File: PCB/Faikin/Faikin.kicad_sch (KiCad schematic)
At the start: 26 parts, among them J1 1x5, J2 Shelly, J3 USB-PROG, Q1 BSS138PS, U2 ESP32-S3-MINI-1, U3 MD8942

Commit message: ERC check fixes
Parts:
- Q1: LCSC Part # C2912548 -> C193381
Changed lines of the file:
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@@
     (effects (font (size 1.27 1.27)) (justify left bottom))
   )
-  (global_label "DC" (shape input) (at 114.935 132.08 0) (fields_autoplaced)
+  (global_label "DC" (shape output) (at 114.935 132.08 0) (fields_autoplaced)
     (effects (font (size 1.27 1.27)) (justify left))
     (property "Intersheetrefs" "${INTERSHEET_REFS}" (at 119.806 132.08 0)
@@
     )
   )
-  (symbol (lib_name "GND_1") (lib_id "power:GND") (at 48.895 81.28 270) (unit 1)
+  (symbol (lib_id "power:GND") (at 48.895 81.28 270) (unit 1)
     (in_bom yes) (on_board yes) (dnp no) (fields_autoplaced)
     (property "Reference" "#PWR01" (at 42.545 81.28 0)
@@
     )
   )
-  (symbol (lib_name "GND_1") (lib_id "power:GND") (at 48.895 76.2 270) (unit 1)
+  (symbol (lib_id "power:GND") (at 48.895 76.2 270) (unit 1)
     (in_bom yes) (on_board yes) (dnp no) (fields_autoplaced)
     (property "Reference" "#PWR01" (at 42.545 76.2 0)
@@
     )
   )
-  (symbol (lib_name "BSS138PS_1") (lib_id "RevK:BSS138PS") (at 123.825 80.645 0) (unit 2)
+  (symbol (lib_id "RevK:BSS138PS") (at 123.825 80.645 0) (unit 2)
     (in_bom yes) (on_board yes) (dnp no)
     (property "Reference" "Q1" (at 122.555 75.565 0)
@@
       (effects (font (size 1.27 1.27)) hide)
     )
-    (property "LCSC Part #" "C2912548" (at 133.35 74.676 0)
+    (property "LCSC Part #" "C193381" (at 133.35 74.676 0)
       (effects (font (size 1.27 1.27)) hide)
     )
@@
     )
   )
-  (symbol (lib_name "GND_1") (lib_id "power:GND") (at 79.375 58.42 90) (unit 1)
+  (symbol (lib_id "power:GND") (at 79.375 58.42 90) (unit 1)
     (in_bom yes) (on_board yes) (dnp no) (fields_autoplaced)
     (property "Reference" "#PWR01" (at 85.725 58.42 0)
@@
     )
   )
-  (symbol (lib_name "GND_1") (lib_id "power:GND") (at 48.895 88.9 270) (unit 1)
+  (symbol (lib_id "power:GND") (at 48.895 88.9 270) (unit 1)
     (in_bom yes) (on_board yes) (dnp no) (fields_autoplaced)
     (property "Reference" "#PWR01" (at 42.545 88.9 0)
@@
     )
   )
-  (symbol (lib_name "GND_1") (lib_id "power:GND") (at 48.895 86.36 270) (unit 1)
+  (symbol (lib_id "power:GND") (at 48.895 86.36 270) (unit 1)
     (in_bom yes) (on_board yes) (dnp no) (fields_autoplaced)
     (property "Reference" "#PWR01" (at 42.545 86.36 0)
@@
       (effects (font (size 1.27 1.27)) hide)
     )
-    (property "LCSC Part #" "C2912548" (at 117.475 94.996 0)
+    (property "LCSC Part #" "C193381" (at 117.475 94.996 0)
       (effects (font (size 1.27 1.27)) hide)
     )
@@
     )
   )
-  (symbol (lib_name "GND_1") (lib_id "power:GND") (at 48.895 83.82 270) (unit 1)
+  (symbol (lib_id "power:GND") (at 48.895 83.82 270) (unit 1)
     (in_bom yes) (on_board yes) (dnp no) (fields_autoplaced)
     (property "Reference" "#PWR01" (at 42.545 83.82 0)
@@
     )
   )
-  (symbol (lib_name "GND_1") (lib_id "power:GND") (at 48.895 91.44 270) (unit 1)
+  (symbol (lib_id "power:GND") (at 48.895 91.44 270) (unit 1)
     (in_bom yes) (on_board yes) (dnp no) (fields_autoplaced)
     (property "Reference" "#PWR01" (at 42.545 91.44 0)
@@
     )
   )
-  (symbol (lib_name "GND_1") (lib_id "power:GND") (at 48.895 78.74 270) (unit 1)
+  (symbol (lib_id "power:GND") (at 48.895 78.74 270) (unit 1)
     (in_bom yes) (on_board yes) (dnp no) (fields_autoplaced)
     (property "Reference" "#PWR01" (at 42.545 78.74 0)

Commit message: 3D
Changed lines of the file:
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@@
   (junction (at 87.63 102.235) (diameter 0) (color 0 0 0 0)
   )
+  (junction (at 112.395 45.72) (diameter 0) (color 0 0 0 0)
+  )
   (junction (at 79.375 53.34) (diameter 0) (color 0 0 0 0)
   )
@@
   )
   (junction (at 146.685 88.9) (diameter 0) (color 0 0 0 0)
+  )
+  (junction (at 130.175 62.865) (diameter 0) (color 0 0 0 0)
   )
   (no_connect (at 79.375 78.74))
@@
     (stroke (width 0) (type default))
   )
+  (wire (pts (xy 107.95 45.72) (xy 112.395 45.72))
+    (stroke (width 0) (type default))
+  )
   (wire (pts (xy 146.685 88.9) (xy 161.29 88.9))
     (stroke (width 0) (type default))
   )
+  (wire (pts (xy 130.175 64.77) (xy 130.175 62.865))
+    (stroke (width 0) (type default))
+  )
+  (wire (pts (xy 130.175 62.865) (xy 130.175 60.96))
+    (stroke (width 0) (type default))
+  )
   (wire (pts (xy 146.685 75.565) (xy 170.815 75.565))
     (stroke (width 0) (type default))
@@
   )
   (wire (pts (xy 139.7 75.565) (xy 139.7 88.9))
+    (stroke (width 0) (type default))
+  )
+  (wire (pts (xy 112.395 45.72) (xy 118.745 45.72))
     (stroke (width 0) (type default))
   )
@@
     )
   )
-  (global_label "DC" (shape input) (at 118.745 45.72 180) (fields_autoplaced)
+  (global_label "DC" (shape input) (at 107.95 45.72 180) (fields_autoplaced)
     (effects (font (size 1.27 1.27)) (justify right))
-    (property "Intersheetrefs" "${INTERSHEET_REFS}" (at 113.9534 45.72 0)
+    (property "Intersheetrefs" "${INTERSHEET_REFS}" (at 103.1584 45.72 0)
       (effects (font (size 1.27 1.27)) (justify right) hide)
     )
@@
         (path "/46c350bb-7de4-4e81-aafd-4af55e37aab0"
           (reference "V5") (unit 1)
+        )
+      )
+    )
+  )
+  (symbol (lib_id "power:PWR_FLAG") (at 130.175 62.865 270) (unit 1)
+    (in_bom yes) (on_board yes) (dnp no) (fields_autoplaced)
+    (property "Reference" "#FLG02" (at 132.08 62.865 0)
+      (effects (font (size 1.27 1.27)) hide)
+    )
+    (property "Value" "PWR_FLAG" (at 133.35 62.865 90)
+      (effects (font (size 1.27 1.27)) (justify left))
+    )
+    (property "Footprint" "" (at 130.175 62.865 0)
+      (effects (font (size 1.27 1.27)) hide)
+    )
+    (property "Datasheet" "~" (at 130.175 62.865 0)
+      (effects (font (size 1.27 1.27)) hide)
+    )
+    (pin "1")
+    (instances
+      (project "Faikin"
+        (path "/46c350bb-7de4-4e81-aafd-4af55e37aab0"
+          (reference "#FLG02") (unit 1)
         )
       )
@@
     )
   )
-  (symbol (lib_id "power:GND") (at 130.175 60.96 0) (unit 1)
+  (symbol (lib_id "power:GND") (at 130.175 64.77 0) (unit 1)
     (in_bom yes) (on_board yes) (dnp no)
-    (property "Reference" "#PWR02" (at 130.175 67.31 0)
-      (effects (font (size 1.27 1.27)) hide)
-    )
-    (property "Value" "GND" (at 130.302 65.3542 0)
-      (effects (font (size 1.27 1.27)))
-    )
-    (property "Footprint" "" (at 130.175 60.96 0)
-      (effects (font (size 1.27 1.27)) hide)
-    )
-    (property "Datasheet" "" (at 130.175 60.96 0)
+    (property "Reference" "#PWR02" (at 130.175 71.12 0)
+      (effects (font (size 1.27 1.27)) hide)
+    )
+    (property "Value" "GND" (at 130.302 69.1642 0)
+      (effects (font (size 1.27 1.27)))
+    )
+    (property "Footprint" "" (at 130.175 64.77 0)
+      (effects (font (size 1.27 1.27)) hide)
+    )
+    (property "Datasheet" "" (at 130.175 64.77 0)
       (effects (font (size 1.27 1.27)) hide)
     )
@@
         )
       )
+    )
+  )
+  (symbol (lib_id "power:PWR_FLAG") (at 112.395 45.72 0) (unit 1)
+    (in_bom yes) (on_board yes) (dnp no) (fields_autoplaced)
+    (property "Reference" "#FLG01" (at 112.395 43.815 0)
+      (effects (font (size 1.27 1.27)) hide)
+    )
+    (property "Value" "PWR_FLAG" (at 112.395 41.5869 0)
+      (effects (font (size 1.27 1.27)))
+    )
+    (property "Footprint" "" (at 112.395 45.72 0)
+      (effects (font (size 1.27 1.27)) hide)
+    )
+    (property "Datasheet" "~" (at 112.395 45.72 0)
+      (effects (font (size 1.27 1.27)) hide)
+    )
+    (pin "1")
+    (instances
+      (project "Faikin"
+        (path "/46c350bb-7de4-4e81-aafd-4af55e37aab0"
+          (reference "#FLG01") (unit 1)
+        )
+      )

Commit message: Tweak
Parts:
- Q1: JLCPCB Rotation Offset -90 -> 180
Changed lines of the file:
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@@
       (effects (font (size 1.27 1.27)) hide)
     )
-    (property "JLCPCB Rotation Offset" "-90" (at 123.825 80.645 0)
+    (property "JLCPCB Rotation Offset" "180" (at 123.825 80.645 0)
       (effects (font (size 1.27 1.27)) hide)
     )
@@
       (effects (font (size 1.27 1.27)) hide)
     )
-    (property "JLCPCB Rotation Offset" "-90" (at 127 100.965 0)
-      (effects (font (size 1.27 1.27)) hide)
-    )
+    (property "JLCPCB Rotation Offset" "180" (at 127 100.965 0)
+      (effects (font (size 1.27 1.27)) hide)
+    )

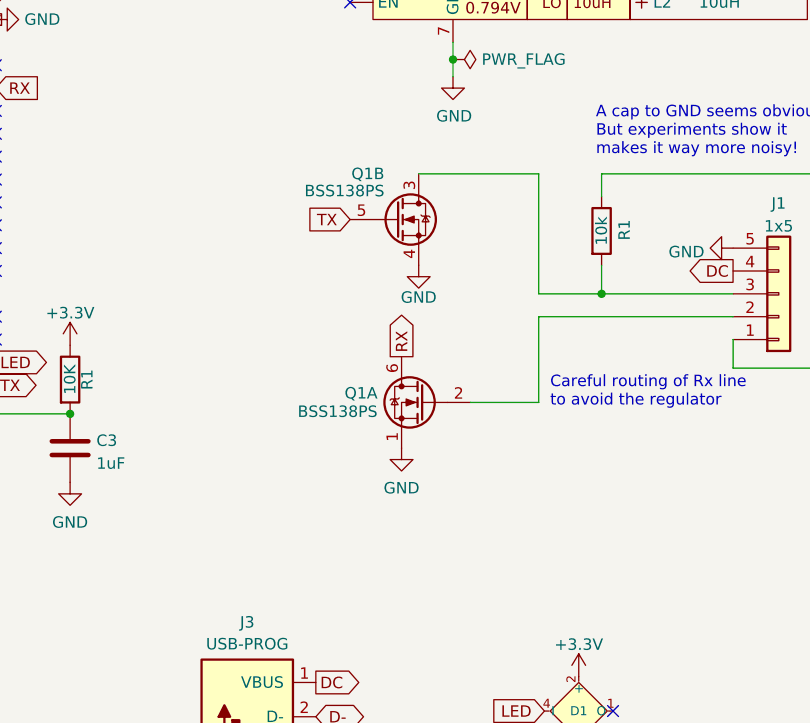
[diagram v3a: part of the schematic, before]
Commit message: ESP diodes
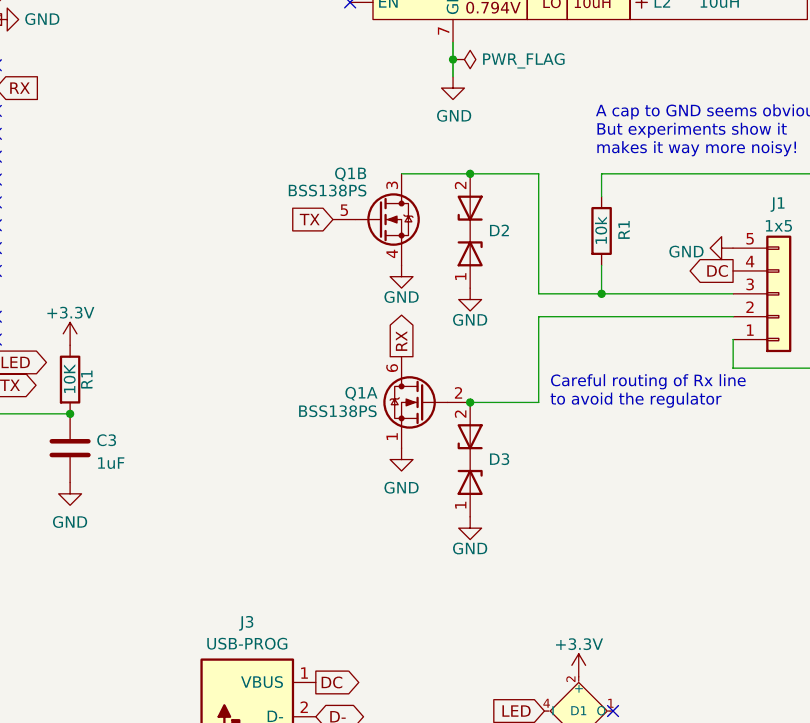
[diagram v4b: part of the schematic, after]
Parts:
- added D2, D3: ~, RevK:DFN1006-2L, symbol RevK:ES05D1MC10
- Q1: JLCPCB Rotation Offset 180 -> -90
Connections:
- net GND: now also D2.1, D3.1
- net at J1.3 (Pin_3), Q1.3 (SP), R1.2: now also D2.2
- net at J1.2 (Pin_2), Q1.2 (GN): now also D3.2
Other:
- moved on the sheet: Q1B
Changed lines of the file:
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@@
   (junction (at 79.375 53.34) (diameter 0) (color 0 0 0 0)
   )
+  (junction (at 132.08 75.565) (diameter 0) (color 0 0 0 0)
+  )
   (junction (at 79.375 58.42) (diameter 0) (color 0 0 0 0)
   )
@@
   )
   (junction (at 130.175 62.865) (diameter 0) (color 0 0 0 0)
+  )
+  (junction (at 132.08 100.965) (diameter 0) (color 0 0 0 0)
   )
   (no_connect (at 79.375 78.74))
@@
     (stroke (width 0) (type default))
   )
-  (wire (pts (xy 126.365 75.565) (xy 139.7 75.565))
-    (stroke (width 0) (type default))
-  )
   (wire (pts (xy 107.95 45.72) (xy 112.395 45.72))
     (stroke (width 0) (type default))
@@
   )
   (wire (pts (xy 161.29 97.155) (xy 170.815 97.155))
+    (stroke (width 0) (type default))
+  )
+  (wire (pts (xy 132.08 75.565) (xy 139.7 75.565))
+    (stroke (width 0) (type default))
+  )
+  (wire (pts (xy 124.46 75.565) (xy 132.08 75.565))
     (stroke (width 0) (type default))
   )
@@
     )
   )
-  (global_label "TX" (shape input) (at 118.745 80.645 180) (fields_autoplaced)
+  (global_label "TX" (shape input) (at 116.84 80.645 180) (fields_autoplaced)
     (effects (font (size 1.27 1.27)) (justify right))
-    (property "Intersheetrefs" "${INTERSHEET_REFS}" (at 114.2437 80.5656 0)
+    (property "Intersheetrefs" "${INTERSHEET_REFS}" (at 112.3387 80.5656 0)
       (effects (font (size 1.27 1.27)) (justify right) hide)
     )
@@
     )
   )
+  (symbol (lib_id "RevK:ES05D1MC10") (at 132.08 107.315 270) (unit 1)
+    (in_bom yes) (on_board yes) (dnp no) (fields_autoplaced)
+    (property "Reference" "D3" (at 134.112 107.315 90)
+      (effects (font (size 1.27 1.27)) (justify left))
+    )
+    (property "Value" "~" (at 132.08 107.315 0)
+      (effects (font (size 1.27 1.27)))
+    )
+    (property "Footprint" "RevK:DFN1006-2L" (at 135.255 107.95 0)
+      (effects (font (size 1.27 1.27)) hide)
+    )
+    (property "Datasheet" "" (at 132.08 107.315 0)
+      (effects (font (size 1.27 1.27)) hide)
+    )
+    (property "LCSC Part #" "C5137770" (at 128.905 107.315 0)
+      (effects (font (size 1.27 1.27)) hide)
+    )
+    (pin "2")
+    (pin "1")
+    (instances
+      (project "Faikin"
+        (path "/46c350bb-7de4-4e81-aafd-4af55e37aab0"
+          (reference "D3") (unit 1)
+        )
+      )
+    )
+  )
   (symbol (lib_id "RevK:VCUT") (at 262.255 171.45 0) (unit 1)
     (in_bom no) (on_board yes) (dnp no) (fields_autoplaced)
@@
     )
   )
-  (symbol (lib_id "RevK:BSS138PS") (at 123.825 80.645 0) (unit 2)
+  (symbol (lib_id "RevK:BSS138PS") (at 121.92 80.645 0) (unit 2)
     (in_bom yes) (on_board yes) (dnp no)
-    (property "Reference" "Q1" (at 122.555 75.565 0)
+    (property "Reference" "Q1" (at 120.65 75.565 0)
       (effects (font (size 1.27 1.27)) (justify right))
     )
-    (property "Value" "BSS138PS" (at 122.555 77.47 0)
+    (property "Value" "BSS138PS" (at 120.65 77.47 0)
       (effects (font (size 1.27 1.27)) (justify right))
     )
-    (property "Footprint" "RevK:SOT-363_SC-70-6" (at 123.825 94.615 0)
+    (property "Footprint" "RevK:SOT-363_SC-70-6" (at 121.92 94.615 0)
       (effects (font (size 1.27 1.27) italic) hide)
     )
-    (property "Datasheet" "https://datasheet.lcsc.com/lcsc/1810011113_Nexperia-BSS138PS-115_C193381.pdf" (at 123.825 67.31 0)
-      (effects (font (size 1.27 1.27)) hide)
-    )
-    (property "LCSC Part #" "C193381" (at 133.35 74.676 0)
-      (effects (font (size 1.27 1.27)) hide)
-    )
-    (property "JLCPCB Rotation Offset" "180" (at 123.825 80.645 0)
+    (property "Datasheet" "https://datasheet.lcsc.com/lcsc/1810011113_Nexperia-BSS138PS-115_C193381.pdf" (at 121.92 67.31 0)
+      (effects (font (size 1.27 1.27)) hide)
+    )
+    (property "LCSC Part #" "C193381" (at 131.445 74.676 0)
+      (effects (font (size 1.27 1.27)) hide)
+    )
+    (property "JLCPCB Rotation Offset" "-90" (at 121.92 80.645 0)
       (effects (font (size 1.27 1.27)) hide)
     )
@@
         (path "/46c350bb-7de4-4e81-aafd-4af55e37aab0"
           (reference "V2") (unit 1)
+        )
+      )
+    )
+  )
+  (symbol (lib_id "RevK:ES05D1MC10") (at 132.08 81.915 270) (unit 1)
+    (in_bom yes) (on_board yes) (dnp no) (fields_autoplaced)
+    (property "Reference" "D2" (at 134.112 81.915 90)
+      (effects (font (size 1.27 1.27)) (justify left))
+    )
+    (property "Value" "~" (at 132.08 81.915 0)
+      (effects (font (size 1.27 1.27)))
+    )
+    (property "Footprint" "RevK:DFN1006-2L" (at 135.255 82.55 0)
+      (effects (font (size 1.27 1.27)) hide)
+    )
+    (property "Datasheet" "" (at 132.08 81.915 0)
+      (effects (font (size 1.27 1.27)) hide)
+    )
+    (property "LCSC Part #" "C5137770" (at 128.905 81.915 0)
+      (effects (font (size 1.27 1.27)) hide)
+    )
+    (pin "2")
+    (pin "1")
+    (instances
+      (project "Faikin"
+        (path "/46c350bb-7de4-4e81-aafd-4af55e37aab0"
+          (reference "D2") (unit 1)
         )
       )
@@
       (effects (font (size 1.27 1.27)) hide)
     )
-    (property "JLCPCB Rotation Offset" "180" (at 127 100.965 0)
+    (property "JLCPCB Rotation Offset" "-90" (at 127 100.965 0)
       (effects (font (size 1.27 1.27)) hide)
     )
@@
     )
   )
+  (symbol (lib_id "power:GND") (at 132.08 113.665 0) (unit 1)
+    (in_bom yes) (on_board yes) (dnp no) (fields_autoplaced)
+    (property "Reference" "#PWR024" (at 132.08 120.015 0)
+      (effects (font (size 1.27 1.27)) hide)
+    )
+    (property "Value" "GND" (at 132.08 117.2408 0)
+      (effects (font (size 1.27 1.27)))
+    )
+    (property "Footprint" "" (at 132.08 113.665 0)
+      (effects (font (size 1.27 1.27)) hide)
+    )
+    (property "Datasheet" "" (at 132.08 113.665 0)
+      (effects (font (size 1.27 1.27)) hide)
+    )
+    (pin "1")
+    (instances
+      (project "Faikin"
+        (path "/46c350bb-7de4-4e81-aafd-4af55e37aab0"
+          (reference "#PWR024") (unit 1)
+        )
+      )
+    )
+  )
   (symbol (lib_id "power:GND") (at 48.895 91.44 270) (unit 1)
     (in_bom yes) (on_board yes) (dnp no) (fields_autoplaced)
@@
     )
   )
-  (symbol (lib_id "power:GND") (at 126.365 85.725 0) (unit 1)
-    (in_bom yes) (on_board yes) (dnp no) (fields_autoplaced)
-    (property "Reference" "#PWR08" (at 126.365 92.075 0)
-      (effects (font (size 1.27 1.27)) hide)
-    )
-    (property "Value" "GND" (at 126.365 89.3008 0)
-      (effects (font (size 1.27 1.27)))
-    )
-    (property "Footprint" "" (at 126.365 85.725 0)
-      (effects (font (size 1.27 1.27)) hide)
-    )
-    (property "Datasheet" "" (at 126.365 85.725 0)
+  (symbol (lib_id "power:GND") (at 124.46 85.725 0) (unit 1)
+    (in_bom yes) (on_board yes) (dnp no) (fields_autoplaced)
+    (property "Reference" "#PWR08" (at 124.46 92.075 0)
+      (effects (font (size 1.27 1.27)) hide)
+    )
+    (property "Value" "GND" (at 124.46 89.3008 0)
+      (effects (font (size 1.27 1.27)))
+    )
+    (property "Footprint" "" (at 124.46 85.725 0)
+      (effects (font (size 1.27 1.27)) hide)
+    )
+    (property "Datasheet" "" (at 124.46 85.725 0)
       (effects (font (size 1.27 1.27)) hide)
     )
@@
         )
       )
+    )
+  )
+  (symbol (lib_id "power:GND") (at 132.08 88.265 0) (unit 1)
+    (in_bom yes) (on_board yes) (dnp no) (fields_autoplaced)
+    (property "Reference" "#PWR03" (at 132.08 94.615 0)
+      (effects (font (size 1.27 1.27)) hide)
+    )
+    (property "Value" "GND" (at 132.08 91.8408 0)
+      (effects (font (size 1.27 1.27)))
+    )
+    (property "Footprint" "" (at 132.08 88.265 0)
+      (effects (font (size 1.27 1.27)) hide)
+    )
+    (property "Datasheet" "" (at 132.08 88.265 0)
+      (effects (font (size 1.27 1.27)) hide)
+    )
+    (pin "1")
+    (instances
+      (project "Faikin"
+        (path "/46c350bb-7de4-4e81-aafd-4af55e37aab0"
+          (reference "#PWR03") (unit 1)
+        )
+      )

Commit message: Production order
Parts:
- Q1: JLCPCB Rotation Offset -90 -> 180
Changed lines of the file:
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@@
       (effects (font (size 1.27 1.27)) hide)
     )
-    (property "JLCPCB Rotation Offset" "-90" (at 121.92 80.645 0)
+    (property "JLCPCB Rotation Offset" "180" (at 121.92 80.645 0)
       (effects (font (size 1.27 1.27)) hide)
     )
@@
       (effects (font (size 1.27 1.27)) hide)
     )
-    (property "JLCPCB Rotation Offset" "-90" (at 127 100.965 0)
-      (effects (font (size 1.27 1.27)) hide)
-    )
+    (property "JLCPCB Rotation Offset" "180" (at 127 100.965 0)
+      (effects (font (size 1.27 1.27)) hide)
+    )
